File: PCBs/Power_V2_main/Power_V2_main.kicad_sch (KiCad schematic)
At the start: 0 parts

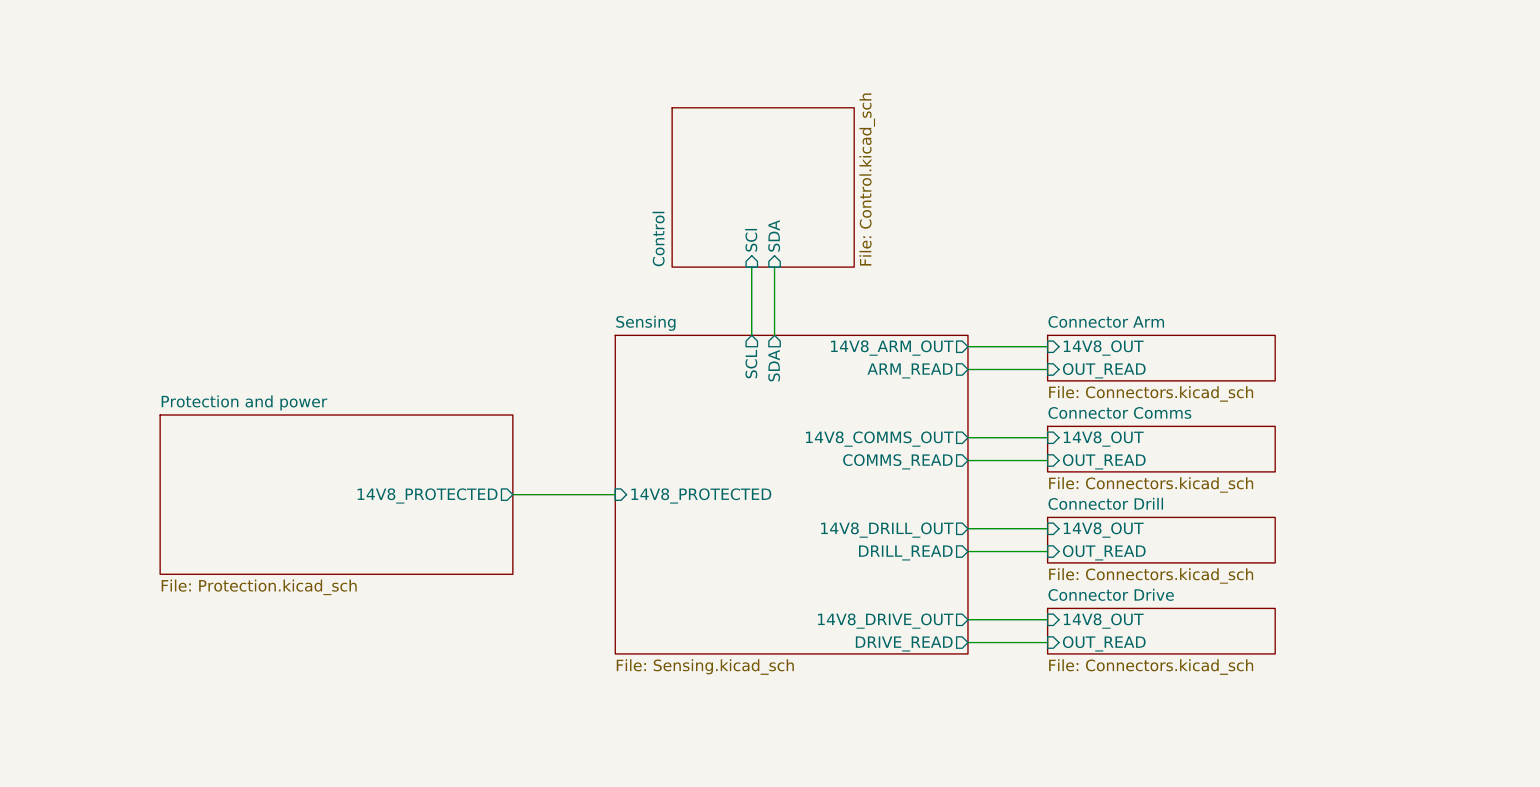
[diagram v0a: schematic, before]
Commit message: shortened main board and secondary
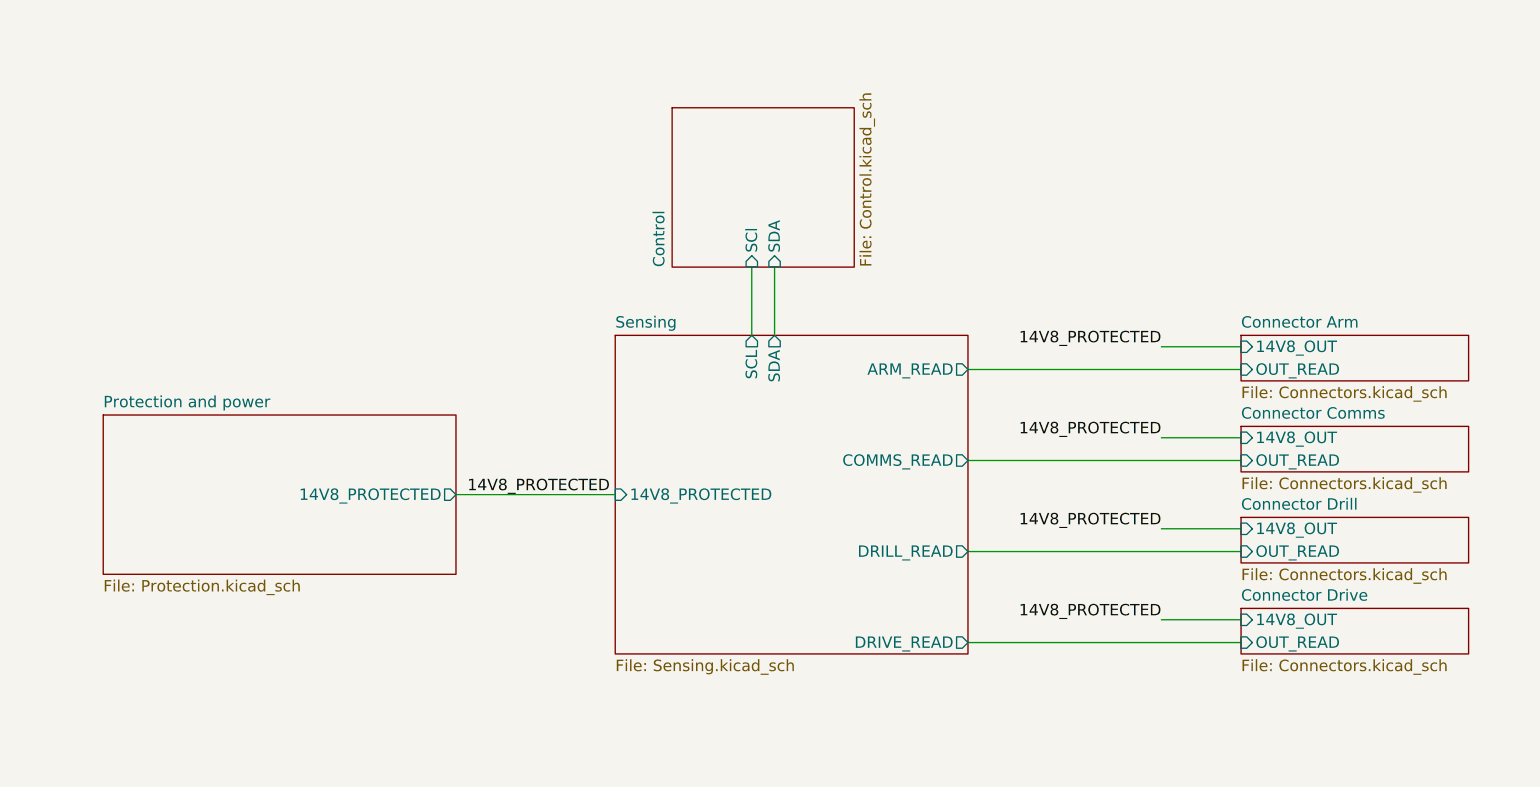
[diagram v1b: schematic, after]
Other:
- sheet Sensing ports: added none; removed 14V8_ARM_OUT, 14V8_COMMS_OUT, 14V8_DRILL_OUT, 14V8_DRIVE_OUT
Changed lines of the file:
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@@
 	(wire
 		(pts
-			(xy 165.1 93.98) (xy 173.99 93.98)
-		)
-		(stroke
-			(width 0)
-			(type default)
-		)
-	)
-	(wire
-		(pts
-			(xy 165.1 114.3) (xy 173.99 114.3)
-		)
-		(stroke
-			(width 0)
-			(type default)
-		)
-	)
-	(wire
-		(pts
-			(xy 114.3 97.79) (xy 125.73 97.79)
-		)
-		(stroke
-			(width 0)
-			(type default)
-		)
-	)
-	(wire
-		(pts
-			(xy 165.1 104.14) (xy 173.99 104.14)
-		)
-		(stroke
-			(width 0)
-			(type default)
-		)
-	)
-	(wire
-		(pts
-			(xy 165.1 83.82) (xy 173.99 83.82)
+			(xy 186.69 81.28) (xy 195.58 81.28)
+		)
+		(stroke
+			(width 0)
+			(type default)
+		)
+	)
+	(wire
+		(pts
+			(xy 165.1 93.98) (xy 195.58 93.98)
+		)
+		(stroke
+			(width 0)
+			(type default)
+		)
+	)
+	(wire
+		(pts
+			(xy 165.1 114.3) (xy 195.58 114.3)
+		)
+		(stroke
+			(width 0)
+			(type default)
+		)
+	)
+	(wire
+		(pts
+			(xy 107.95 97.79) (xy 125.73 97.79)
+		)
+		(stroke
+			(width 0)
+			(type default)
+		)
+	)
+	(wire
+		(pts
+			(xy 165.1 104.14) (xy 195.58 104.14)
+		)
+		(stroke
+			(width 0)
+			(type default)
+		)
+	)
+	(wire
+		(pts
+			(xy 186.69 111.76) (xy 195.58 111.76)
+		)
+		(stroke
+			(width 0)
+			(type default)
+		)
+	)
+	(wire
+		(pts
+			(xy 165.1 83.82) (xy 195.58 83.82)
 		)
 		(stroke
@@
 	(wire
 		(pts
-			(xy 165.1 101.6) (xy 173.99 101.6)
+			(xy 186.69 91.44) (xy 195.58 91.44)
+		)
+		(stroke
+			(width 0)
+			(type default)
+		)
+	)
+	(wire
+		(pts
+			(xy 186.69 101.6) (xy 195.58 101.6)
 		)
 		(stroke
@@
 		)
 	)
-	(wire
-		(pts
-			(xy 165.1 81.28) (xy 173.99 81.28)
-		)
-		(stroke
-			(width 0)
-			(type default)
-		)
-	)
-	(wire
-		(pts
-			(xy 165.1 111.76) (xy 173.99 111.76)
-		)
-		(stroke
-			(width 0)
-			(type default)
-		)
-	)
-	(wire
-		(pts
-			(xy 165.1 91.44) (xy 173.99 91.44)
-		)
-		(stroke
-			(width 0)
-			(type default)
-		)
-	)
-	(sheet
-		(at 173.99 90.17)
+	(label "14V8_PROTECTED"
+		(at 186.69 91.44 180)
+		(effects
+			(font
+				(size 1.27 1.27)
+			)
+			(justify right bottom)
+		)
+	)
+	(label "14V8_PROTECTED"
+		(at 186.69 81.28 180)
+		(effects
+			(font
+				(size 1.27 1.27)
+			)
+			(justify right bottom)
+		)
+	)
+	(label "14V8_PROTECTED"
+		(at 109.22 97.79 0)
+		(effects
+			(font
+				(size 1.27 1.27)
+			)
+			(justify left bottom)
+		)
+	)
+	(label "14V8_PROTECTED"
+		(at 186.69 101.6 180)
+		(effects
+			(font
+				(size 1.27 1.27)
+			)
+			(justify right bottom)
+		)
+	)
+	(label "14V8_PROTECTED"
+		(at 186.69 111.76 180)
+		(effects
+			(font
+				(size 1.27 1.27)
+			)
+			(justify right bottom)
+		)
+	)
+	(sheet
+		(at 195.58 90.17)
 		(size 25.4 5.08)
 		(exclude_from_sim no)
@@
 		)
 		(property "Sheetname" "Connector Comms"
-			(at 173.99 89.4584 0)
+			(at 195.58 89.4584 0)
 			(effects
 				(font
@@
 		)
 		(property "Sheetfile" "Connectors.kicad_sch"
-			(at 173.99 95.8346 0)
+			(at 195.58 95.8346 0)
 			(effects
 				(font
@@
 		)
 		(pin "14V8_OUT" input
-			(at 173.99 91.44 180)
+			(at 195.58 91.44 180)
 			(effects
 				(font
@@
 		)
 		(pin "OUT_READ" input
-			(at 173.99 93.98 180)
+			(at 195.58 93.98 180)
 			(effects
 				(font
@@
 			)
 		)
-		(pin "14V8_ARM_OUT" output
-			(at 165.1 81.28 0)
-			(effects
-				(font
-					(size 1.27 1.27)
-				)
-				(justify right)
-			)
-		)
-		(pin "14V8_COMMS_OUT" output
-			(at 165.1 91.44 0)
-			(effects
-				(font
-					(size 1.27 1.27)
-				)
-				(justify right)
-			)
-		)
-		(pin "14V8_DRILL_OUT" output
-			(at 165.1 101.6 0)
-			(effects
-				(font
-					(size 1.27 1.27)
-				)
-				(justify right)
-			)
-		)
-		(pin "14V8_DRIVE_OUT" output
-			(at 165.1 111.76 0)
-			(effects
-				(font
-					(size 1.27 1.27)
-				)
-				(justify right)
-			)
-		)
 		(pin "14V8_PROTECTED" input
 			(at 125.73 97.79 180)
@@
 	)
 	(sheet
-		(at 173.99 80.01)
+		(at 195.58 80.01)
 		(size 25.4 5.08)
 		(exclude_from_sim no)
@@
 		)
 		(property "Sheetname" "Connector Arm"
-			(at 173.99 79.2984 0)
+			(at 195.58 79.2984 0)
 			(effects
 				(font
@@
 		)
 		(property "Sheetfile" "Connectors.kicad_sch"
-			(at 173.99 85.6746 0)
+			(at 195.58 85.6746 0)
 			(effects
 				(font
@@
 		)
 		(pin "14V8_OUT" input
-			(at 173.99 81.28 180)
+			(at 195.58 81.28 180)
 			(effects
 				(font
@@
 		)
 		(pin "OUT_READ" input
-			(at 173.99 83.82 180)
+			(at 195.58 83.82 180)
 			(effects
 				(font
@@
 	)
 	(sheet
-		(at 173.99 110.49)
+		(at 195.58 110.49)
 		(size 25.4 5.08)
 		(exclude_from_sim no)
@@
 		)
 		(property "Sheetname" "Connector Drive"
-			(at 173.99 109.7784 0)
+			(at 195.58 109.7784 0)
 			(effects
 				(font
@@
 		)
 		(property "Sheetfile" "Connectors.kicad_sch"
-			(at 173.99 116.1546 0)
+			(at 195.58 116.1546 0)
 			(effects
 				(font
@@
 		)
 		(pin "14V8_OUT" input
-			(at 173.99 111.76 180)
+			(at 195.58 111.76 180)
 			(effects
 				(font
@@
 		)
 		(pin "OUT_READ" input
-			(at 173.99 114.3 180)
+			(at 195.58 114.3 180)
 			(effects
 				(font
@@
 	)
 	(sheet
-		(at 173.99 100.33)
+		(at 195.58 100.33)
 		(size 25.4 5.08)
 		(exclude_from_sim no)
@@
 		)
 		(property "Sheetname" "Connector Drill"
-			(at 173.99 99.6184 0)
+			(at 195.58 99.6184 0)
 			(effects
 				(font
@@
 		)
 		(property "Sheetfile" "Connectors.kicad_sch"
-			(at 173.99 105.9946 0)
+			(at 195.58 105.9946 0)
 			(effects
 				(font
@@
 		)
 		(pin "14V8_OUT" input
-			(at 173.99 101.6 180)
+			(at 195.58 101.6 180)
 			(effects
 				(font
@@
 		)
 		(pin "OUT_READ" input
-			(at 173.99 104.14 180)
+			(at 195.58 104.14 180)
 			(effects
 				(font
@@
 	)
 	(sheet
-		(at 74.93 88.9)
+		(at 68.58 88.9)
 		(size 39.37 17.78)
 		(exclude_from_sim no)
@@
 		)
 		(property "Sheetname" "Protection and power"
-			(at 74.93 88.1884 0)
+			(at 68.58 88.1884 0)
 			(effects
 				(font
@@
 		)
 		(property "Sheetfile" "Protection.kicad_sch"
-			(at 74.93 107.2646 0)
+			(at 68.58 107.2646 0)
 			(effects
 				(font
@@
 		)
 		(pin "14V8_PROTECTED" output
-			(at 114.3 97.79 0)
-			(effects
-				(font
+			(at 107.95 97.79 0)
+			(effects
+				(font

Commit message: main schematic for power board main
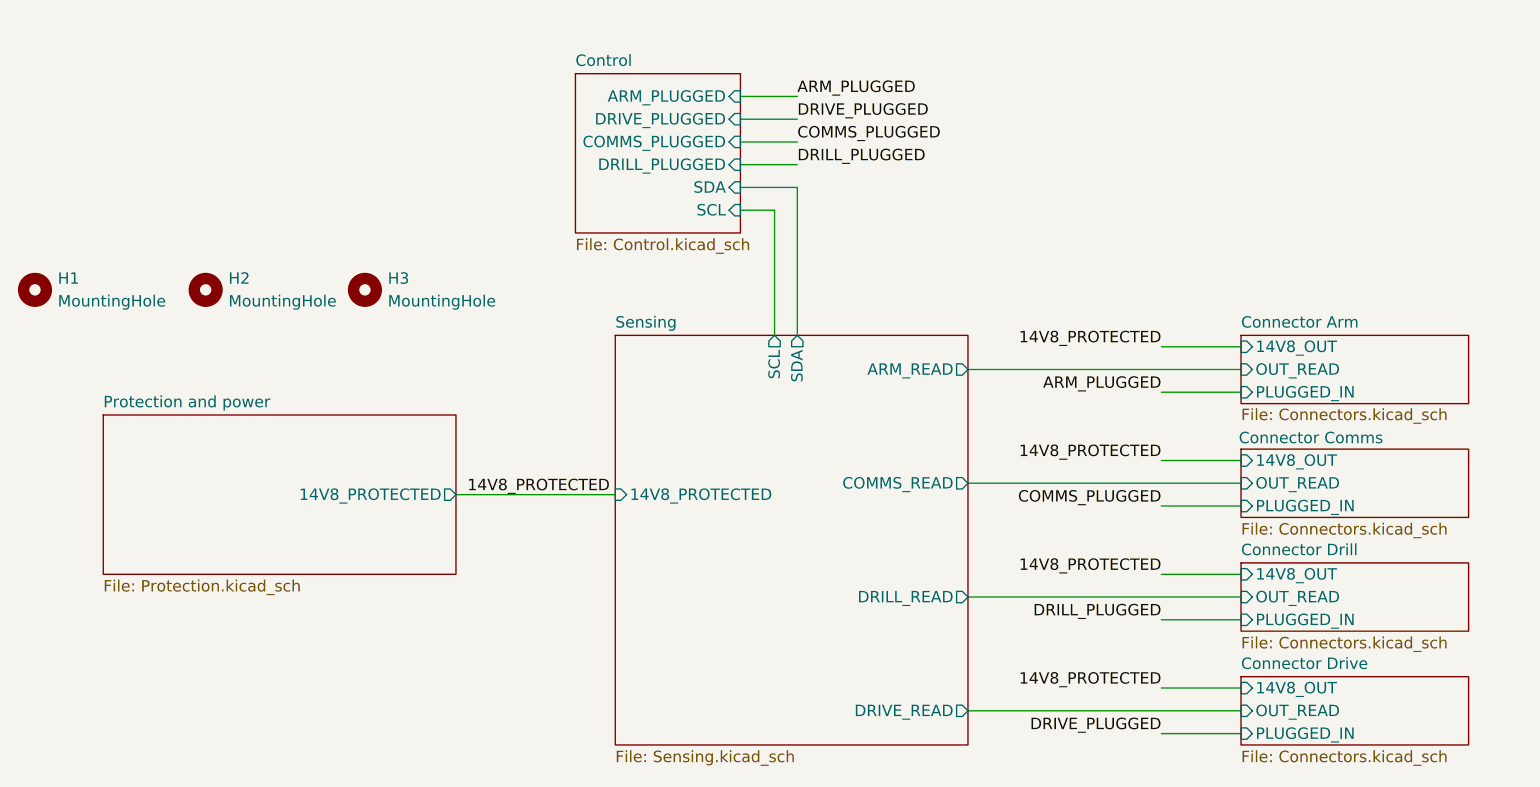
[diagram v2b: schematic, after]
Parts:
- added H1, H2, H3: MountingHole, MountingHole:MountingHole_2.5mm, symbol Mechanical:MountingHole
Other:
- sheet Connector Arm ports: added PLUGGED_IN; removed none
- sheet Connector Comms ports: added PLUGGED_IN; removed none
- sheet Connector Drill ports: added PLUGGED_IN; removed none
- sheet Connector Drive ports: added PLUGGED_IN; removed none
- sheet Control ports: added ARM_PLUGGED, COMMS_PLUGGED, DRILL_PLUGGED, DRIVE_PLUGGED, SCL; removed SCl

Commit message: a 5 hour binge of PCB layout on the main
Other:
- sheet Connector Arm ports: added none; removed PLUGGED_IN
- sheet Connector Comms ports: added none; removed PLUGGED_IN
- sheet Connector Drill ports: added none; removed PLUGGED_IN
- sheet Connector Drive ports: added none; removed PLUGGED_IN
- sheet Control ports: added none; removed ARM_PLUGGED, COMMS_PLUGGED, DRILL_PLUGGED, DRIVE_PLUGGED
